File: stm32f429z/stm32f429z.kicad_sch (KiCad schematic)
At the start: 8 parts, among them SW1 Boot0, SW2 NRST, U1 STM32F429ZITx

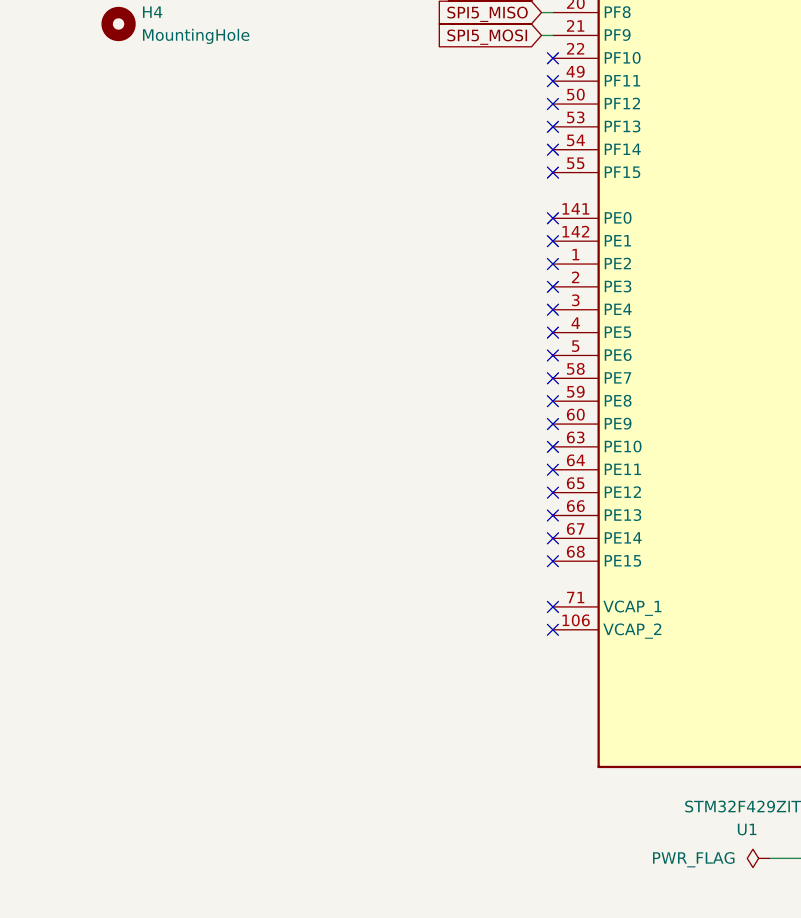
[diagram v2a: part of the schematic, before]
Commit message: changed logging schematic, tweaked some parts of the schematic
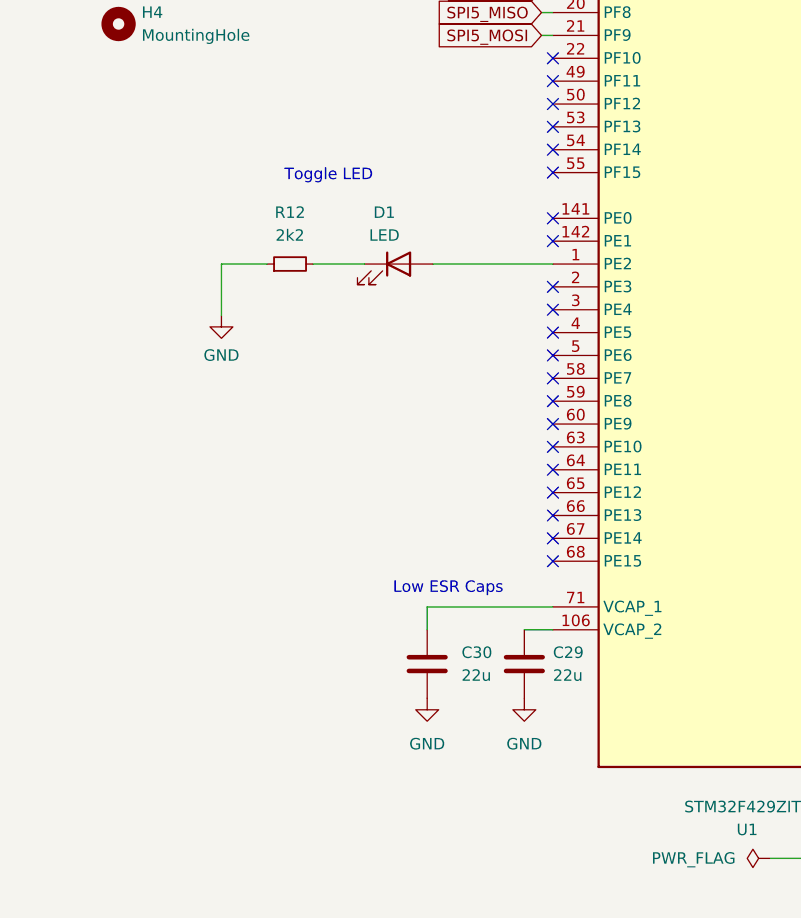
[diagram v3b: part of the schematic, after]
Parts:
- added C29, C30: 22u, Capacitor_SMD:C_0603_1608Metric_Pad1.08x0.95mm_HandSolder, symbol Device:C
- added D1: LED, LED_SMD:LED_0603_1608Metric_Pad1.05x0.95mm_HandSolder, symbol Device:LED
- added R12: 2k2, Resistor_SMD:R_0603_1608Metric_Pad0.98x0.95mm_HandSolder, symbol Device:R_Small
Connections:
- net GND: now also C29.2, C30.2, R12.1
- net at U1.1 (PE2): now also D1.2 (A)
- net at U1.106 (VCAP_2): now also C29.1
- net at U1.71 (VCAP_1): now also C30.1
- new net: D1.1 (K), R12.2
- no-connect marks 70 -> 67
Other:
- note added: "Low ESR Caps"
- note added: "Toggle LED"
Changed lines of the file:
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@@
   (no_connect (at 76.2 134.62))
   (no_connect (at 76.2 81.28))
-  (no_connect (at 76.2 213.36))
   (no_connect (at 76.2 119.38))
   (no_connect (at 137.16 147.32))
@@
   (no_connect (at 137.16 76.2))
   (no_connect (at 137.16 142.24))
-  (no_connect (at 76.2 172.72))
   (no_connect (at 137.16 198.12))
   (no_connect (at 76.2 162.56))
@@
   (no_connect (at 76.2 198.12))
   (no_connect (at 76.2 180.34))
-  (no_connect (at 76.2 210.82))
   (no_connect (at 137.16 160.02))
   (no_connect (at 76.2 149.86))
@@
     (stroke (width 0) (type default))
   )
+  (wire (pts (xy 49.53 172.72) (xy 55.245 172.72))
+    (stroke (width 0) (type default))
+  )
   (wire (pts (xy 109.22 48.26) (xy 109.22 44.45))
     (stroke (width 0) (type default))
@@
     (stroke (width 0) (type default))
   )
+  (wire (pts (xy 62.23 213.36) (xy 62.23 210.82))
+    (stroke (width 0) (type default))
+  )
   (wire (pts (xy 20.32 104.14) (xy 26.67 104.14))
     (stroke (width 0) (type default))
@@
     (stroke (width 0) (type default))
   )
+  (wire (pts (xy 62.23 210.82) (xy 76.2 210.82))
+    (stroke (width 0) (type default))
+  )
   (wire (pts (xy 106.68 44.45) (xy 109.22 44.45))
     (stroke (width 0) (type default))
   )
+  (wire (pts (xy 73.025 213.36) (xy 76.2 213.36))
+    (stroke (width 0) (type default))
+  )
   (wire (pts (xy 20.32 102.87) (xy 20.32 104.14))
     (stroke (width 0) (type default))
@@
     (stroke (width 0) (type default))
   )
+  (wire (pts (xy 44.45 172.72) (xy 39.37 172.72))
+    (stroke (width 0) (type default))
+  )
   (wire (pts (xy 109.22 44.45) (xy 111.76 44.45))
     (stroke (width 0) (type default))
@@
     (stroke (width 0) (type default))
   )
+  (wire (pts (xy 62.865 172.72) (xy 76.2 172.72))
+    (stroke (width 0) (type default))
+  )
   (wire (pts (xy 66.04 68.58) (xy 76.2 68.58))
     (stroke (width 0) (type default))
@@
     (stroke (width 0) (type default))
   )
+  (wire (pts (xy 39.37 172.72) (xy 39.37 178.435))
+    (stroke (width 0) (type default))
+  )
   (wire (pts (xy 111.76 48.26) (xy 111.76 44.45))
     (stroke (width 0) (type default))
@@
   (wire (pts (xy 74.93 142.24) (xy 76.2 142.24))
     (stroke (width 0) (type default))
+  )
+  (text "Toggle LED\n\n" (at 46.355 165.735 0)
+    (effects (font (size 1.27 1.27)) (justify left bottom))
+  )
+  (text "Low ESR Caps\n" (at 58.42 209.55 0)
+    (effects (font (size 1.27 1.27)) (justify left bottom))
   )
   (global_label "SPI3_CS  " (shape input) (at 76.2 104.14 180) (fields_autoplaced)
@@
     )
   )
+  (symbol (lib_id "power:GND") (at 62.23 220.98 0) (unit 1)
+    (in_bom yes) (on_board yes) (dnp no) (fields_autoplaced)
+    (property "Reference" "#PWR074" (at 62.23 227.33 0)
+      (effects (font (size 1.27 1.27)) hide)
+    )
+    (property "Value" "GND" (at 62.23 226.06 0)
+      (effects (font (size 1.27 1.27)))
+    )
+    (property "Footprint" "" (at 62.23 220.98 0)
+      (effects (font (size 1.27 1.27)) hide)
+    )
+    (property "Datasheet" "" (at 62.23 220.98 0)
+      (effects (font (size 1.27 1.27)) hide)
+    )
+    (pin "1")
+    (instances
+      (project "stm32f429z"
+        (path "/09c21947-d3c4-4f82-9fb4-45f647ba61fc"
+          (reference "#PWR074") (unit 1)
+        )
+      )
+    )
+  )
   (symbol (lib_id "power:GND") (at 35.56 82.55 0) (unit 1)
     (in_bom yes) (on_board yes) (dnp no) (fields_autoplaced)
@@
         (path "/09c21947-d3c4-4f82-9fb4-45f647ba61fc"
           (reference "#PWR054") (unit 1)
+        )
+      )
+    )
+  )
+  (symbol (lib_id "Device:C") (at 62.23 217.17 0) (unit 1)
+    (in_bom yes) (on_board yes) (dnp no) (fields_autoplaced)
+    (property "Reference" "C30" (at 66.04 215.9 0)
+      (effects (font (size 1.27 1.27)) (justify left))
+    )
+    (property "Value" "22u" (at 66.04 218.44 0)
+      (effects (font (size 1.27 1.27)) (justify left))
+    )
+    (property "Footprint" "Capacitor_SMD:C_0603_1608Metric_Pad1.08x0.95mm_HandSolder" (at 63.1952 220.98 0)
+      (effects (font (size 1.27 1.27)) hide)
+    )
+    (property "Datasheet" "~" (at 62.23 217.17 0)
+      (effects (font (size 1.27 1.27)) hide)
+    )
+    (pin "1")
+    (pin "2")
+    (instances
+      (project "stm32f429z"
+        (path "/09c21947-d3c4-4f82-9fb4-45f647ba61fc"
+          (reference "C30") (unit 1)
         )
       )
@@
     )
   )
+  (symbol (lib_id "Device:R_Small") (at 46.99 172.72 90) (unit 1)
+    (in_bom yes) (on_board yes) (dnp no) (fields_autoplaced)
+    (property "Reference" "R12" (at 46.99 167.005 90)
+      (effects (font (size 1.27 1.27)))
+    )
+    (property "Value" "2k2" (at 46.99 169.545 90)
+      (effects (font (size 1.27 1.27)))
+    )
+    (property "Footprint" "Resistor_SMD:R_0603_1608Metric_Pad0.98x0.95mm_HandSolder" (at 46.99 172.72 0)
+      (effects (font (size 1.27 1.27)) hide)
+    )
+    (property "Datasheet" "~" (at 46.99 172.72 0)
+      (effects (font (size 1.27 1.27)) hide)
+    )
+    (pin "1")
+    (pin "2")
+    (instances
+      (project "stm32f429z"
+        (path "/09c21947-d3c4-4f82-9fb4-45f647ba61fc/a8b40fa5-269b-4c25-b32b-052a9524b109"
+          (reference "R12") (unit 1)
+        )
+        (path "/09c21947-d3c4-4f82-9fb4-45f647ba61fc/694a836f-d3f6-4b1c-8285-62a6284055e0"
+          (reference "R16") (unit 1)
+        )
+        (path "/09c21947-d3c4-4f82-9fb4-45f647ba61fc"
+          (reference "R17") (unit 1)
+        )
+      )
+    )
+  )
   (symbol (lib_id "power:+3.3V") (at 20.32 102.87 0) (unit 1)
     (in_bom yes) (on_board yes) (dnp no) (fields_autoplaced)
@@
         (path "/09c21947-d3c4-4f82-9fb4-45f647ba61fc"
           (reference "#PWR053") (unit 1)
+        )
+      )
+    )
+  )
+  (symbol (lib_id "Device:C") (at 73.025 217.17 0) (unit 1)
+    (in_bom yes) (on_board yes) (dnp no) (fields_autoplaced)
+    (property "Reference" "C29" (at 76.2 215.9 0)
+      (effects (font (size 1.27 1.27)) (justify left))
+    )
+    (property "Value" "22u" (at 76.2 218.44 0)
+      (effects (font (size 1.27 1.27)) (justify left))
+    )
+    (property "Footprint" "Capacitor_SMD:C_0603_1608Metric_Pad1.08x0.95mm_HandSolder" (at 73.9902 220.98 0)
+      (effects (font (size 1.27 1.27)) hide)
+    )
+    (property "Datasheet" "~" (at 73.025 217.17 0)
+      (effects (font (size 1.27 1.27)) hide)
+    )
+    (pin "1")
+    (pin "2")
+    (instances
+      (project "stm32f429z"
+        (path "/09c21947-d3c4-4f82-9fb4-45f647ba61fc"
+          (reference "C29") (unit 1)
+        )
+      )
+    )
+  )
+  (symbol (lib_id "Device:LED") (at 59.055 172.72 0) (unit 1)
+    (in_bom yes) (on_board yes) (dnp no) (fields_autoplaced)
+    (property "Reference" "D1" (at 57.4675 167.005 0)
+      (effects (font (size 1.27 1.27)))
+    )
+    (property "Value" "LED" (at 57.4675 169.545 0)
+      (effects (font (size 1.27 1.27)))
+    )
+    (property "Footprint" "LED_SMD:LED_0603_1608Metric_Pad1.05x0.95mm_HandSolder" (at 59.055 172.72 0)
+      (effects (font (size 1.27 1.27)) hide)
+    )
+    (property "Datasheet" "~" (at 59.055 172.72 0)
+      (effects (font (size 1.27 1.27)) hide)
+    )
+    (pin "1")
+    (pin "2")
+    (instances
+      (project "stm32f429z"
+        (path "/09c21947-d3c4-4f82-9fb4-45f647ba61fc"
+          (reference "D1") (unit 1)
         )
       )
@@
     )
   )
+  (symbol (lib_id "power:GND") (at 39.37 178.435 0) (unit 1)
+    (in_bom yes) (on_board yes) (dnp no) (fields_autoplaced)
+    (property "Reference" "#PWR047" (at 39.37 184.785 0)
+      (effects (font (size 1.27 1.27)) hide)
+    )
+    (property "Value" "GND" (at 39.37 182.88 0)
+      (effects (font (size 1.27 1.27)))
+    )
+    (property "Footprint" "" (at 39.37 178.435 0)
+      (effects (font (size 1.27 1.27)) hide)
+    )
+    (property "Datasheet" "" (at 39.37 178.435 0)
+      (effects (font (size 1.27 1.27)) hide)
+    )
+    (pin "1")
+    (instances
+      (project "stm32f429z"
+        (path "/09c21947-d3c4-4f82-9fb4-45f647ba61fc"
+          (reference "#PWR047") (unit 1)
+        )
+      )
+    )
+  )
   (symbol (lib_id "Mechanical:MountingHole") (at 27.94 146.05 0) (unit 1)
     (in_bom yes) (on_board yes) (dnp no) (fields_autoplaced)
@@
         )
       )
+    )
+  )
+  (symbol (lib_id "power:GND") (at 73.025 220.98 0) (unit 1)
+    (in_bom yes) (on_board yes) (dnp no) (fields_autoplaced)
+    (property "Reference" "#PWR075" (at 73.025 227.33 0)
+      (effects (font (size 1.27 1.27)) hide)
+    )
+    (property "Value" "GND" (at 73.025 226.06 0)
+      (effects (font (size 1.27 1.27)))
+    )
+    (property "Footprint" "" (at 73.025 220.98 0)
+      (effects (font (size 1.27 1.27)) hide)
+    )
+    (property "Datasheet" "" (at 73.025 220.98 0)
+      (effects (font (size 1.27 1.27)) hide)
+    )
+    (pin "1")
+    (instances
+      (project "stm32f429z"
+        (path "/09c21947-d3c4-4f82-9fb4-45f647ba61fc"
+          (reference "#PWR075") (unit 1)
+        )
+      )

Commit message: usb footprint changes, Silkscreen markers for pin 1 in ICs and polarity for other components. Edited excel BOM list and kicad list for BOM cost.
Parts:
- C22: JLCpart# (none) -> C76599
- C29, C30: JLCpart# (none) -> C96446
- D1: JLCpart# (none) -> C72038
- R12: JLCpart# (none) -> C427273
- U1: JLCpart# (none) -> C92002
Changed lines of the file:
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@@
+      (effects (font (size 1.27 1.27)) hide)
+    )
+    (property "JLCpart#" "" (at 31.75 104.14 0)
       (effects (font (size 1.27 1.27)) hide)
     )
@@
     )
     (property "Datasheet" "~" (at 62.23 217.17 0)
+      (effects (font (size 1.27 1.27)) hide)
+    )
+    (property "JLCpart#" "C96446" (at 62.23 217.17 0)
       (effects (font (size 1.27 1.27)) hide)
     )
@@
     )
     (property "Datasheet" "https://www.st.com/resource/en/datasheet/stm32f429zi.pdf" (at 106.68 142.24 0)
+      (effects (font (size 1.27 1.27)) hide)
+    )
+    (property "JLCpart#" "C92002" (at 106.68 142.24 0)
       (effects (font (size 1.27 1.27)) hide)
     )
@@
       (effects (font (size 1.27 1.27)) hide)
     )
+    (property "JLCpart#" "" (at 27.94 127 0)
+      (effects (font (size 1.27 1.27)) hide)
+    )
     (instances
       (project "stm32f429z"
@@
       (effects (font (size 1.27 1.27)) hide)
     )
+    (property "JLCpart#" "" (at 27.94 133.35 0)
+      (effects (font (size 1.27 1.27)) hide)
+    )
     (instances
       (project "stm32f429z"
@@
     )
     (property "Datasheet" "~" (at 46.99 172.72 0)
+      (effects (font (size 1.27 1.27)) hide)
+    )
+    (property "JLCpart#" "C427273" (at 46.99 172.72 0)
       (effects (font (size 1.27 1.27)) hide)
     )
@@
       (effects (font (size 1.27 1.27)) hide)
     )
+    (property "JLCpart#" "C96446" (at 73.025 217.17 0)
+      (effects (font (size 1.27 1.27)) hide)
+    )
     (pin "1")
     (pin "2")
@@
     )
     (property "Datasheet" "~" (at 59.055 172.72 0)
+      (effects (font (size 1.27 1.27)) hide)
+    )
+    (property "JLCpart#" "C72038" (at 59.055 172.72 0)
       (effects (font (size 1.27 1.27)) hide)
     )
@@
       (effects (font (size 1.27 1.27)) hide)
     )
+    (property "JLCpart#" "" (at 27.94 73.66 0)
+      (effects (font (size 1.27 1.27)) hide)
+    )
     (pin "1")
     (pin "2")
@@
       (effects (font (size 1.27 1.27)) hide)
     )
+    (property "JLCpart#" "" (at 27.94 146.05 0)
+      (effects (font (size 1.27 1.27)) hide)
+    )
     (instances
       (project "stm32f429z"
@@
       (effects (font (size 1.27 1.27)) hide)
     )
+    (property "JLCpart#" "C76599" (at 35.56 73.66 0)
+      (effects (font (size 1.27 1.27)) hide)
+    )
     (pin "1")
     (pin "2")
@@
       (effects (font (size 1.27 1.27)) hide)
     )
+    (property "JLCpart#" "" (at 27.94 139.7 0)
+      (effects (font (size 1.27 1.27)) hide)
+    )

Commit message: updated some stuff
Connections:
- net +3.3V: now also SW1.1 (A); no longer SW1.2 (B)
- net BOOT0: now also SW1.2 (B); no longer SW1.1 (A)
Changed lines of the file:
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@@
-    (stroke (width 0) (type default))
-  )
-  (wire (pts (xy 20.32 104.14) (xy 26.67 104.14))
     (stroke (width 0) (type default))
   )
@@
     (stroke (width 0) (type default))
   )
-  (wire (pts (xy 20.32 102.87) (xy 20.32 104.14))
-    (stroke (width 0) (type default))
-  )
   (wire (pts (xy 73.66 76.2) (xy 76.2 76.2))
     (stroke (width 0) (type default))
@@
     (stroke (width 0) (type default))
   )
+  (wire (pts (xy 36.83 107.95) (xy 36.83 106.68))
+    (stroke (width 0) (type default))
+  )
   (wire (pts (xy 104.14 44.45) (xy 106.68 44.45))
     (stroke (width 0) (type default))
@@
     (stroke (width 0) (type default))
   )
+  (wire (pts (xy 24.13 104.14) (xy 26.67 104.14))
+    (stroke (width 0) (type default))
+  )
   (wire (pts (xy 111.76 44.45) (xy 114.3 44.45))
     (stroke (width 0) (type default))
@@
   )
   (wire (pts (xy 91.44 39.37) (xy 91.44 44.45))
+    (stroke (width 0) (type default))
+  )
+  (wire (pts (xy 36.83 100.33) (xy 36.83 101.6))
     (stroke (width 0) (type default))
   )
@@
     )
   )
-  (global_label "BOOT0" (shape input) (at 36.83 101.6 0) (fields_autoplaced)
-    (effects (font (size 1.27 1.27)) (justify left))
-    (property "Intersheetrefs" "${INTERSHEET_REFS}" (at 45.9233 101.6 0)
-      (effects (font (size 1.27 1.27)) (justify left) hide)
-    )
-  )
   (global_label "ADC1_IN14" (shape input) (at 137.16 152.4 0) (fields_autoplaced)
     (effects (font (size 1.27 1.27)) (justify left))
@@
     (property "Intersheetrefs" "${INTERSHEET_REFS}" (at 150.8495 220.98 0)
       (effects (font (size 1.27 1.27)) (justify left) hide)
+    )
+  )
+  (global_label "BOOT0" (shape input) (at 24.13 104.14 180) (fields_autoplaced)
+    (effects (font (size 1.27 1.27)) (justify right))
+    (property "Intersheetrefs" "${INTERSHEET_REFS}" (at 15.0367 104.14 0)
+      (effects (font (size 1.27 1.27)) (justify right) hide)
     )
   )
@@
     )
   )
-  (symbol (lib_id "power:+3.3V") (at 20.32 102.87 0) (unit 1)
-    (in_bom yes) (on_board yes) (dnp no) (fields_autoplaced)
-    (property "Reference" "#PWR053" (at 20.32 106.68 0)
-      (effects (font (size 1.27 1.27)) hide)
-    )
-    (property "Value" "+3.3V" (at 20.32 97.79 0)
-      (effects (font (size 1.27 1.27)))
-    )
-    (property "Footprint" "" (at 20.32 102.87 0)
-      (effects (font (size 1.27 1.27)) hide)
-    )
-    (property "Datasheet" "" (at 20.32 102.87 0)
-      (effects (font (size 1.27 1.27)) hide)
-    )
-    (pin "1")
-    (instances
-      (project "stm32f429z"
-        (path "/09c21947-d3c4-4f82-9fb4-45f647ba61fc"
-          (reference "#PWR053") (unit 1)
-        )
-      )
-    )
-  )
   (symbol (lib_id "Device:C") (at 73.025 217.17 0) (unit 1)
     (in_bom yes) (on_board yes) (dnp no) (fields_autoplaced)
@@
     )
   )
-  (symbol (lib_id "power:GND") (at 36.83 106.68 0) (unit 1)
-    (in_bom yes) (on_board yes) (dnp no) (fields_autoplaced)
-    (property "Reference" "#PWR052" (at 36.83 113.03 0)
-      (effects (font (size 1.27 1.27)) hide)
-    )
-    (property "Value" "GND" (at 36.83 111.76 0)
-      (effects (font (size 1.27 1.27)))
-    )
-    (property "Footprint" "" (at 36.83 106.68 0)
-      (effects (font (size 1.27 1.27)) hide)
-    )
-    (property "Datasheet" "" (at 36.83 106.68 0)
+  (symbol (lib_id "power:GND") (at 36.83 107.95 0) (unit 1)
+    (in_bom yes) (on_board yes) (dnp no) (fields_autoplaced)
+    (property "Reference" "#PWR052" (at 36.83 114.3 0)
+      (effects (font (size 1.27 1.27)) hide)
+    )
+    (property "Value" "GND" (at 36.83 113.03 0)
+      (effects (font (size 1.27 1.27)))
+    )
+    (property "Footprint" "" (at 36.83 107.95 0)
+      (effects (font (size 1.27 1.27)) hide)
+    )
+    (property "Datasheet" "" (at 36.83 107.95 0)
       (effects (font (size 1.27 1.27)) hide)
     )
@@
         )
       )
+    )
+  )
+  (symbol (lib_id "power:+3.3V") (at 36.83 100.33 0) (unit 1)
+    (in_bom yes) (on_board yes) (dnp no) (fields_autoplaced)
+    (property "Reference" "#PWR053" (at 36.83 104.14 0)
+      (effects (font (size 1.27 1.27)) hide)
+    )
+    (property "Value" "+3.3V" (at 36.83 95.25 0)
+      (effects (font (size 1.27 1.27)))
+    )
+    (property "Footprint" "" (at 36.83 100.33 0)
+      (effects (font (size 1.27 1.27)) hide)
+    )
+    (property "Datasheet" "" (at 36.83 100.33 0)
+      (effects (font (size 1.27 1.27)) hide)
+    )
+    (pin "1")
+    (instances
+      (project "stm32f429z"
+        (path "/09c21947-d3c4-4f82-9fb4-45f647ba61fc"
+          (reference "#PWR053") (unit 1)
+        )
+      )
